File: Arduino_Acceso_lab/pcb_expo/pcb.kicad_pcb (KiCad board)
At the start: 2 copper layers, 88.4 x 55.4 mm, 15 parts, among them P1 modulo wifi, P20 CONN_01X02, U1 LM2576

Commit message: Versión corregida por DJB del Shield Wifi para Arduini Mega.
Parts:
- R1, R2, R3, R4, R5: footprint Resistors_ThroughHole:Resistor_Horizontal_RM7mm -> Resistors_ThroughHole:Resistor_Horizontal_RM10mm
- moved P20 31.9 mm to (114.8, 121.5)
- moved C3 28.8 mm to (147.0, 93.5), turned to 270 degrees
- moved R5 26.5 mm to (116.0, 98.5), turned to 90 degrees
- moved D1 23.3 mm to (132.5, 93.0), turned to 270 degrees
- moved C1 18.9 mm to (125.5, 123.0)
- moved D2 18.7 mm to (127.0, 111.0), turned to 0 degrees
- moved R4 18.6 mm to (120.0, 88.5), turned to 270 degrees
- moved L1 14.0 mm to (127.0, 105.0), turned to 90 degrees
- moved R1 14.0 mm to (127.5, 88.5)
- moved U1 9.40 mm to (115.5, 107.0)
- moved R3 8.72 mm to (171.5, 96.0)
- moved C2 8.43 mm to (139.5, 93.3), turned to 270 degrees
- moved R2 7.12 mm to (181.5, 92.0)
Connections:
- net /3.3 renamed +3.3VP
- C2 pad 1: Net-(C2-Pad1) -> +9V
- C3 pad 1: Net-(C2-Pad1) -> +9V
- L1 pad 2: Net-(C2-Pad1) -> +9V
- P1 pad 2: /RXwifi -> /TXwifi2
- R1 pad 1: Net-(C2-Pad1) -> +9V
- R2 pad 2: /TXwifi -> /RXwifi
- R4 pad 1: Net-(R4-Pad1) -> +9V
- R4 pad 2: +9V -> Net-(R4-Pad2)
- R5 pad 1: +9V -> Net-(R4-Pad2)
- R5 pad 2: Net-(R5-Pad2) -> GND
- SH1 pad 18: /TXwifi -> /RXwifi
- SH1 pad 19: /RXwifi -> /TXwifi2
- U1 pad 3: Net-(U1-Pad3) -> GND
- U1 pad 4: Net-(R4-Pad1) -> Net-(R4-Pad2)
- U1 pad 5: Net-(U1-Pad3) -> GND
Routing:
- net Net-(C1-Pad1): track 78.9 -> 30.3 mm, vias 4 -> 2
- net /TXwifi2: track 0.00 -> 48.3 mm
- net Net-(C2-Pad1): track 47.3 -> 0.00 mm
- net /TXwifi: track 40.0 -> 0.00 mm
- net /RXwifi: track 47.2 -> 13.7 mm
- net +9V: track 60.4 -> 87.7 mm
- net Net-(R4-Pad1): track 14.4 -> 0.00 mm
- net Net-(R4-Pad2): track 0.00 -> 12.1 mm
- net Net-(D2-Pad1): track 29.8 -> 25.2 mm
- net GND: track 4.32 -> 0.00 mm
- net Net-(U1-Pad3): track 3.50 -> 0.00 mm
- net Net-(D1-Pad2): track 9.67 -> 7.15 mm
- net Net-(P1-Pad7): track 10.8 -> 9.37 mm
- net +3.3VP: track 88.0 -> 88.6 mm, vias 2 -> 0
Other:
- board size 88.4 x 55.4 mm -> 88.8 x 55.5 mm
- board text added: "+12V"
- board text added: "+9V"
- board text added: "3.3V"
- board text added: "MG-LAB"
- board text added: "TX Wifi"
- board text added: "^GND"

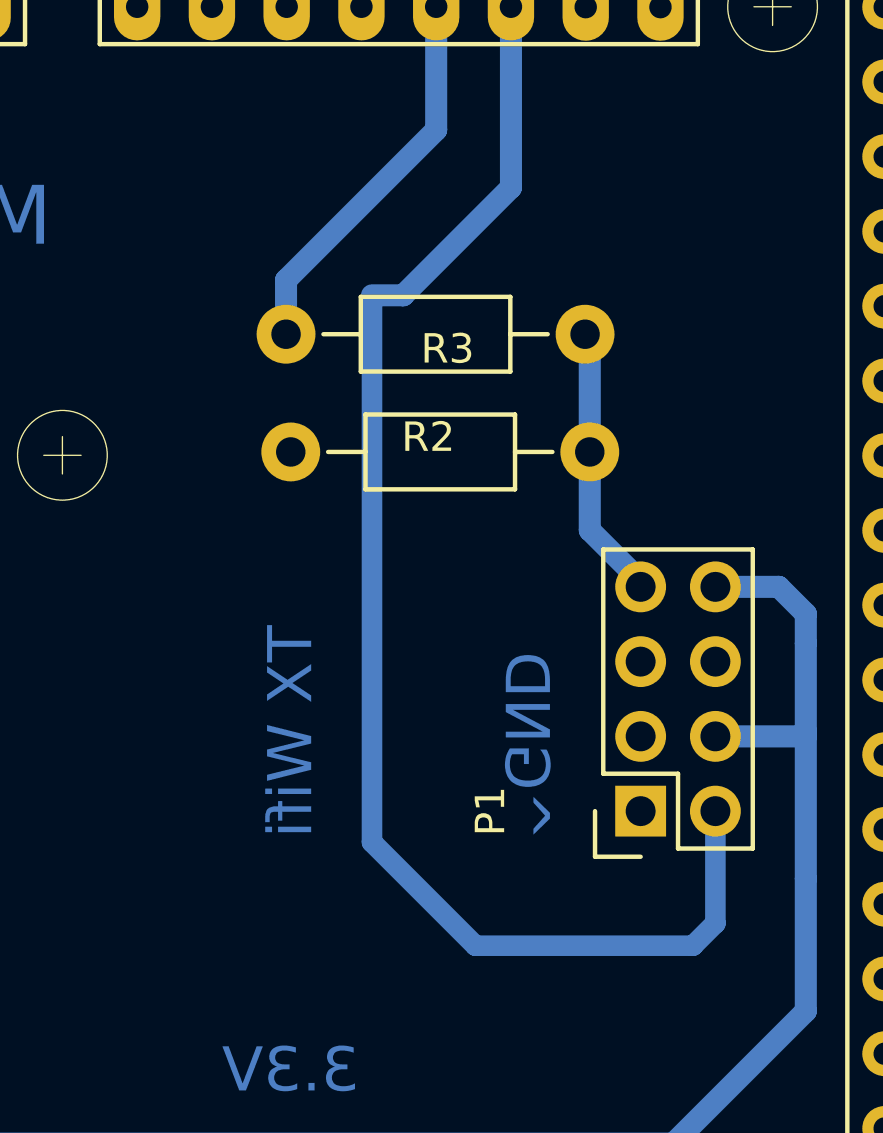
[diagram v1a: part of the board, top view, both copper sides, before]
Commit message: Detalles Arduino Mega Wifi Shield.
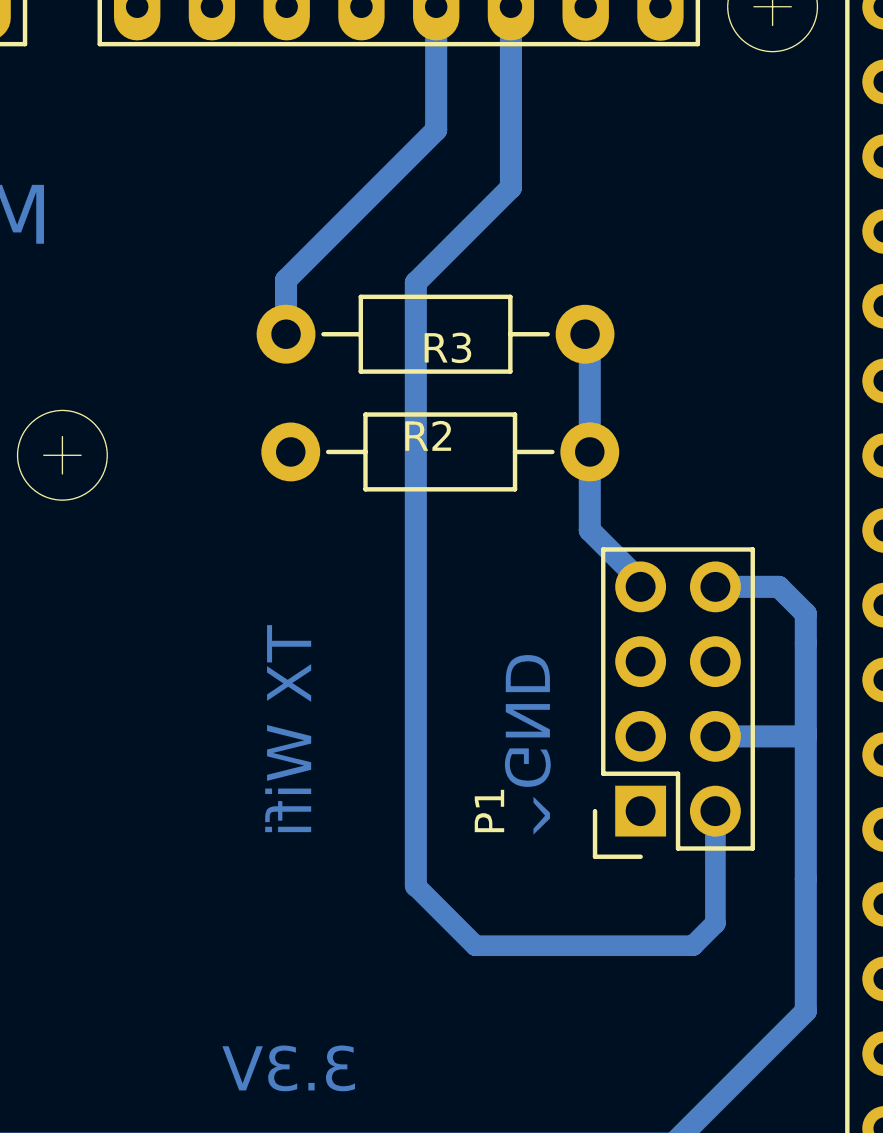
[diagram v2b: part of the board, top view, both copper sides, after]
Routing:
- net /TXwifi2: track 48.3 -> 46.5 mm
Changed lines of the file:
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@@
-(kicad_pcb (version 4) (host pcbnew 4.0.3+e1-6302~38~ubuntu14.04.1-stable)
+(kicad_pcb (version 4) (host pcbnew 4.0.2+dfsg1-2~bpo8+1-stable)
   (general
     (links 30)
@@
     (thickness 1.6)
     (drawings 12)
-    (tracks 89)
+    (tracks 88)
     (zones 0)
     (modules 15)
@@
     (pad_drill 3.048)
     (pad_to_mask_clearance 0)
-    (aux_axis_origin 103.378 121.666)
+    (aux_axis_origin 108.25 133.5)
+    (grid_origin 108.5 133.5)
     (visible_elements 7FFEFFFF)
     (pcbplotparams
@@
   (segment (start 124.96 102.46) (end 123.5 101) (width 0.75) (layer B.Cu) (net 89))
   (segment (start 143.002 128.7272) (end 143.4211 129.1463) (width 0.7) (layer B.Cu) (net 89))
-  (segment (start 174.26 90.678) (end 175.322 90.678) (width 0.75) (layer B.Cu) (net 90))
+  (segment (start 175.75 110.75) (end 175.75 90.25) (width 0.75) (layer B.Cu) (net 90))
   (segment (start 185.166 112.776) (end 185.928 112.014) (width 0.7) (layer B.Cu) (net 90))
   (segment (start 177.776 112.776) (end 185.166 112.776) (width 0.7) (layer B.Cu) (net 90))
-  (segment (start 174.26 109.26) (end 177.776 112.776) (width 0.7) (layer B.Cu) (net 90))
-  (segment (start 174.26 90.678) (end 174.26 109.26) (width 0.7) (layer B.Cu) (net 90))
+  (segment (start 175.75 110.75) (end 177.776 112.776) (width 0.7) (layer B.Cu) (net 90))
   (segment (start 185.928 108.204) (end 185.928 112.014) (width 0.7) (layer B.Cu) (net 90))
   (segment (start 178.9811 87.0189) (end 178.9811 80.8736) (width 0.75) (layer B.Cu) (net 90))
-  (segment (start 175.322 90.678) (end 178.9811 87.0189) (width 0.75) (layer B.Cu) (net 90))
+  (segment (start 175.75 90.25) (end 178.9811 87.0189) (width 0.75) (layer B.Cu) (net 90))
   (segment (start 179.07 80.9625) (end 178.9811 80.8736) (width 0.7) (layer B.Cu) (net 90))
   (segment (start 185.928 105.664) (end 189 105.664) (width 0.75) (layer B.Cu) (net 91))
